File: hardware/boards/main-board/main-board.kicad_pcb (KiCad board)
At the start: 4 copper layers, 292.4 x 42 mm, 142 parts, among them J1 2x12 1.27mm shrouded box head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, J2 1x5, J4 12-way, J5 12-way, J6 8-way 2.54mm right-angle pin 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, Q1 AO3401A, SW1 KS-33, SW2 KS-33, SW3 KS-33, SW4 KS-33, SW5 KS-33, SW6 KS-33, SW7 KS-33, SW8 KS-33, U1 SP0504BAHT or equivalent 4-ch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, U10 MPXV4006DP, U2 MCP3202-CI/SN, U3 OPA2197IDR, U4 REF5050IDR, U5 R-78E5.0-1.0, U6 74AHCT125, U7 74HCS165, U8 74HCS165, U9 SP0504BAHTG 4-channel 5V array

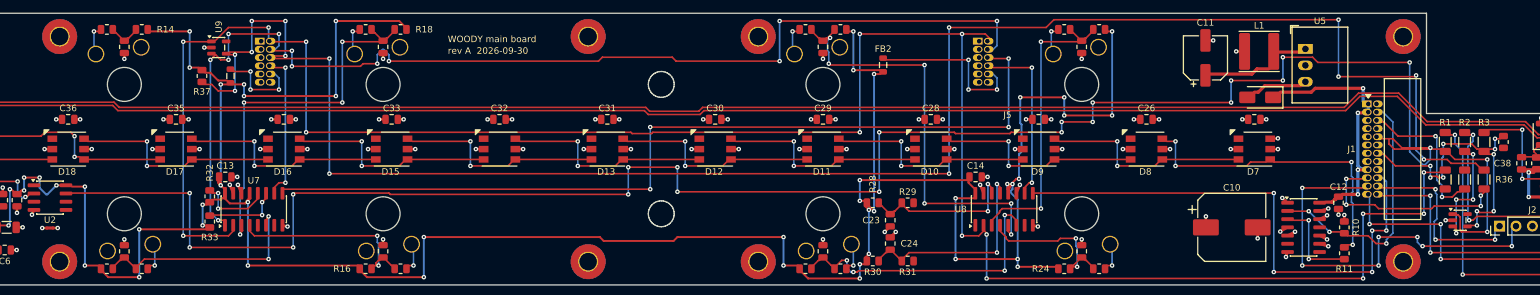
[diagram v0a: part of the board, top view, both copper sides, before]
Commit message: Main board after finish: 12 left
Co-Authored-By: Claude Opus 5.5 <noreply@anthropic.com>
Claude-Session: https://claude.ai/code/session_01LmB4muFXnoLprWX4JzuJ5A
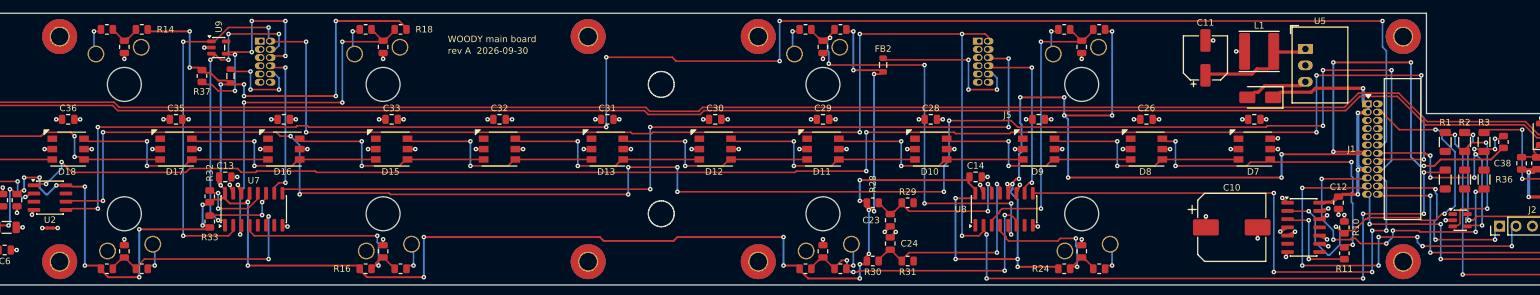
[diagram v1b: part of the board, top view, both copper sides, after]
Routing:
- net /IO35: track 314.6 -> 0.00 mm, vias 22 -> 0
- net /IO37: track 0.00 -> 266.8 mm, vias 0 -> 13
- net /IO36: track 16.3 -> 273.3 mm, vias 4 -> 9
- net /IO39: track 0.00 -> 251.7 mm, vias 0 -> 8
- net /CHAIN_SER_LH: track 280.8 -> 32.0 mm, vias 14 -> 6
- net /CHAIN_SHLD: track 172.6 -> 44.0 mm, vias 12 -> 5
- net DEV_3V3: track 418.1 -> 537.3 mm, vias 48 -> 55
- net /IO7: track 22.3 -> 0.00 mm, vias 2 -> 0
- net /IO1: track 36.7 -> 58.4 mm, vias 3 -> 4
- net /IO33: track 30.3 -> 47.4 mm, vias 4 -> 6
- net /carrier/IO34: track 42.6 -> 40.4 mm, vias 10 -> 8

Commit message: Main board after finish with rip_up 6: 5 left
Co-Authored-By: Claude Opus 5.5 <noreply@anthropic.com>
Claude-Session: https://claude.ai/code/session_01LmB4muFXnoLprWX4JzuJ5A
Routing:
- net /IO35: track 0.00 -> 254.4 mm, vias 0 -> 9
- net /CHAIN_SER_LH: track 32.0 -> 268.6 mm, vias 6 -> 22
- net /CHAIN_SCK: track 321.9 -> 143.2 mm, vias 15 -> 11
- net /CHAIN_SHLD: track 44.0 -> 157.9 mm, vias 5 -> 9
- net /KEY_LT2: track 2.66 -> 55.5 mm, vias 0 -> 4
- net /carrier/IO34: track 40.4 -> 87.9 mm, vias 8 -> 11
- net /IO39: track 251.7 -> 279.5 mm, vias 8 -> 16
- net /IO36: track 273.3 -> 297.4 mm, vias 9 -> 18
- net /IO7: track 0.00 -> 21.5 mm, vias 0 -> 4
- net /IO38: track 0.00 -> 19.5 mm, vias 0 -> 2
- net /IO33: track 47.4 -> 32.1 mm, vias 6 -> 4
- net /U0RXD: track 61.8 -> 49.1 mm
- net /IO37: track 266.8 -> 279.0 mm, vias 13 -> 20
- net /U0TXD: track 27.2 -> 22.4 mm, vias 3 -> 1
- net DEV_3V3: track 537.3 -> 533.5 mm, vias 55 -> 62
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
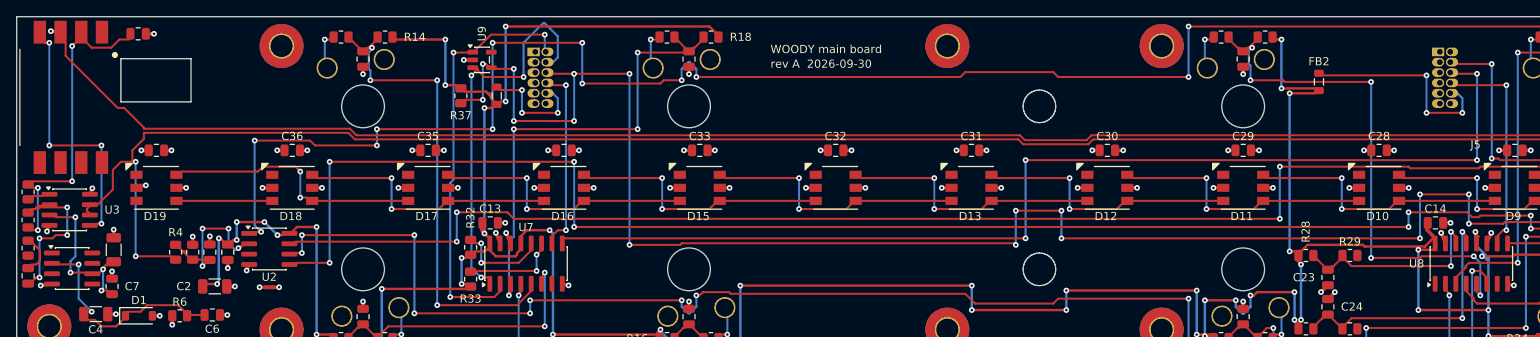
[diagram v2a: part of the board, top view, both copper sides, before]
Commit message: Main board: feedback column stacked as its ring (R7, R9, C9, R8), every connection routed; 3 track-shape errors on CHAIN_SHLD left
Co-Authored-By: Claude Opus 5.5 <noreply@anthropic.com>
Claude-Session: https://claude.ai/code/session_01LmB4muFXnoLprWX4JzuJ5A
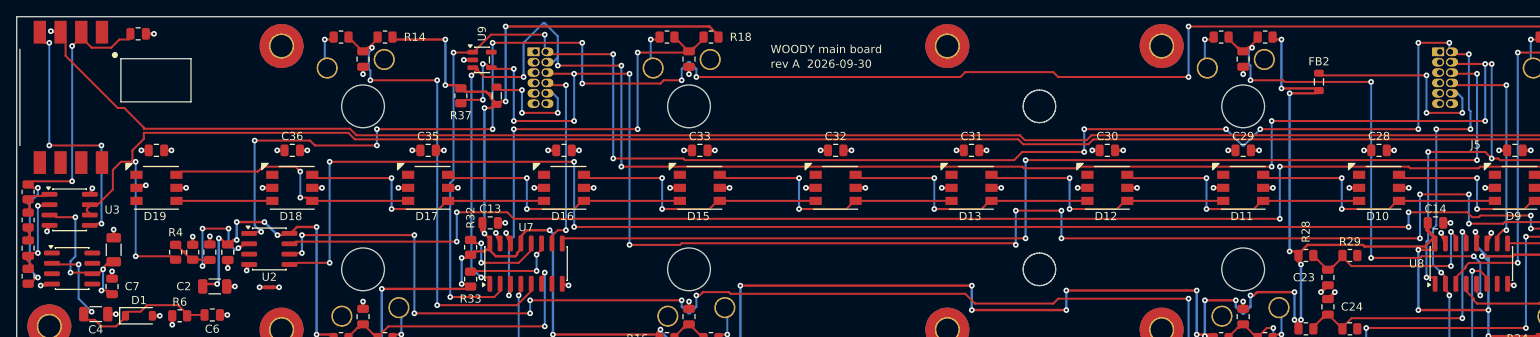
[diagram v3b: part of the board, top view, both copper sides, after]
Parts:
- moved R8 6.90 mm to (68.9, 132.3)
- moved R9 3.45 mm to (68.9, 125.5), turned to -90 degrees
- moved C9 3.40 mm to (68.9, 128.9)
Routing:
- net /CHAIN_SCK: track 143.2 -> 316.7 mm, vias 11 -> 24
- net /CHAIN_SHLD: track 157.9 -> 325.4 mm, vias 9 -> 18
- net /breath-excitation-reference/REF_MINUS: track 18.3 -> 8.13 mm, vias 4 -> 2
- net VS: track 34.2 -> 41.0 mm
- net /breath-excitation-reference/AC_FB_MID: track 3.70 -> 1.05 mm
- net /breath-excitation-reference/BUF_OUT: track 1.20 -> 2.25 mm

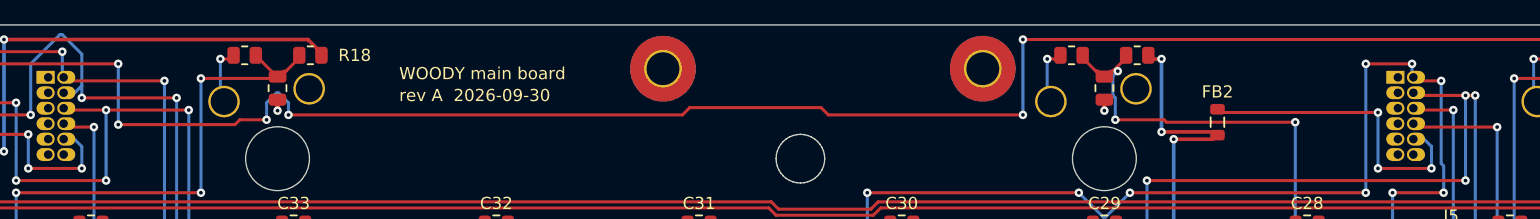
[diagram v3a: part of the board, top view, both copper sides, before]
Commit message: Main board: pcb.py check 0 errors - every connection routed, DRC clean, planes and island checks pass; tidy runs on a fresh load after complete
Co-Authored-By: Claude Opus 5.5 <noreply@anthropic.com>
Claude-Session: https://claude.ai/code/session_01LmB4muFXnoLprWX4JzuJ5A
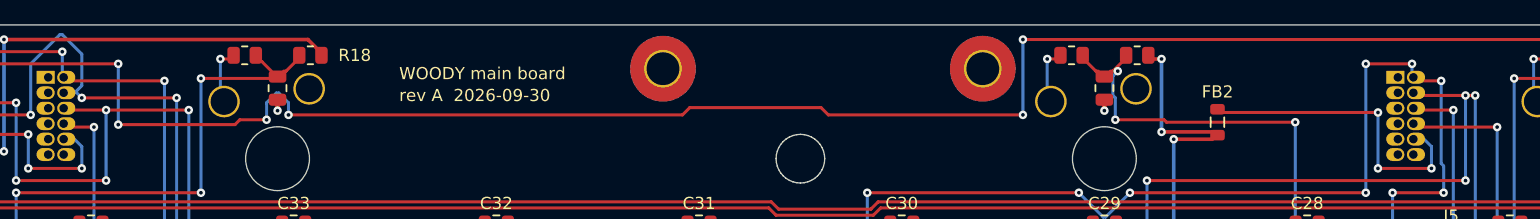
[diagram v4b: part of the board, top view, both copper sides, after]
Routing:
- net /CHAIN_SHLD: track 325.4 -> 321.7 mm
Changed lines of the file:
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@@
-	)
-	(segment
-		(start 247.7 106.3)
-		(end 244.3 106.3)
-		(width 0.25)
-		(layer "F.Cu")
-		(net 6)
 	)
 	(segment
@@
 	(segment
 		(start 133.3 106.1)
-		(end 133.9 105.5)
+		(end 133.4 106)
 		(width 0.25)
 		(layer "B.Cu")
@@
 	)
 	(segment
+		(start 133.4 106)
+		(end 133.9 105.5)
+		(width 0.25)
+		(layer "B.Cu")
+		(net 6)
+	)
+	(segment
 		(start 133.9 105.5)
 		(end 133.9 102.9)
@@
 	)
 	(segment
-		(start 133.9 105.5)
+		(start 133.4 106)
 		(end 133.9 106.5)
 		(width 0.25)

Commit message: Main board re-laid out with the F1 parts: 10 left before finish
Co-Authored-By: Claude Opus 5.5 <noreply@anthropic.com>
Claude-Session: https://claude.ai/code/session_01LmB4muFXnoLprWX4JzuJ5A
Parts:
- added C201: 1uF, Capacitor_SMD:C_0805_2012Metric, F.Cu at (88.9, 102.6)
- added C202: 10nF, Capacitor_SMD:C_0805_2012Metric, F.Cu at (82.4, 102.6)
- added C203: 470pF, Capacitor_SMD:C_0805_2012Metric, F.Cu at (81.8, 126.4)
- added C204: 100nF, Capacitor_SMD:C_0805_2012Metric, F.Cu at (79.2, 125.0)
- moved C8 3.50 mm to (85.9, 102.6)
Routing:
- net /IO36: track 297.4 -> 0.00 mm, vias 18 -> 0
- net /IO37: track 279.0 -> 0.00 mm, vias 20 -> 0
- net /CHAIN_SER_LH: track 268.6 -> 28.0 mm, vias 22 -> 6
- net /IO35: track 254.4 -> 16.6 mm, vias 9 -> 2
- net /carrier/IO34: track 87.9 -> 13.8 mm, vias 11 -> 4
- net /IO39: track 279.5 -> 232.9 mm, vias 16 -> 6
- net /IO33: track 32.1 -> 76.2 mm, vias 4 -> 6
- net /IO1: track 61.6 -> 43.1 mm, vias 7 -> 3
- net /KEY_FREE2: track 10.4 -> 23.4 mm, vias 2 -> 4
- net /U0RXD: track 49.1 -> 61.8 mm
- net /EN: track 37.8 -> 29.4 mm, vias 3 -> 2
- net DEV_3V3: track 533.5 -> 527.0 mm, vias 62 -> 54
- net /CHAIN_SCK: track 316.7 -> 321.9 mm, vias 24 -> 15
- net AGND_INST: track 307.7 -> 312.7 mm, vias 15 -> 19
- net /led-strip-drive/LED_DI: track 45.3 -> 41.5 mm
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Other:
- board text added: "C201"
- board text added: "D4"
- board text added: "FB1"
- board text added: "R35"
- board text added: "U1"
- board text added: "U6"

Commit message: Main board after finish with the F1 parts: 5 left
Co-Authored-By: Claude Opus 5.5 <noreply@anthropic.com>
Claude-Session: https://claude.ai/code/session_01LmB4muFXnoLprWX4JzuJ5A
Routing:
- net /CHAIN_SER_LH: track 28.0 -> 299.8 mm, vias 6 -> 22
- net /IO37: track 0.00 -> 263.0 mm, vias 0 -> 13
- net DEV_3V3: track 527.0 -> 475.0 mm, vias 54 -> 50
- net /IO36: track 0.00 -> 29.7 mm, vias 0 -> 2
- net /carrier/IO34: track 13.8 -> 34.2 mm
- net /IO1: track 43.1 -> 54.7 mm
- net /CHAIN_SHLD: track 318.3 -> 310.8 mm
- net /IO35: track 16.6 -> 21.0 mm
- net /CHAIN_QH_RT: track 81.4 -> 78.9 mm, vias 5 -> 3
- net /U0RXD: track 61.8 -> 63.0 mm, vias 7 -> 5

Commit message: Main board re-laid out with R44: 13 left before finish
Co-Authored-By: Claude Opus 5.5 <noreply@anthropic.com>
Claude-Session: https://claude.ai/code/session_01LmB4muFXnoLprWX4JzuJ5A
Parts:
- added R44: 2k2 1%, Resistor_SMD:R_0603_1608Metric, F.Cu at (136.9, 128.3)
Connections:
- U7 pad 9: /HOP_LT_RH -> /HOP_LT_QH
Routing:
- net /IO37: track 263.0 -> 0.00 mm, vias 13 -> 0
- net /IO35: track 21.0 -> 272.9 mm, vias 2 -> 12
- net /IO36: track 29.7 -> 270.8 mm, vias 2 -> 12
- net /CHAIN_SER_LH: track 299.8 -> 68.3 mm, vias 22 -> 10
- net /CHAIN_SCK: track 321.9 -> 153.7 mm, vias 15 -> 8
- net /CHAIN_SHLD: track 310.8 -> 222.7 mm, vias 26 -> 17
- net /CHAIN_QH_RT: track 78.9 -> 0.00 mm, vias 3 -> 0
- net /KEY_RT2: track 62.6 -> 2.66 mm, vias 6 -> 0
- net /KEY_LT2: track 55.5 -> 2.66 mm, vias 4 -> 0
- net /IO39: track 232.9 -> 272.3 mm, vias 6 -> 12
- net /IO38: track 18.8 -> 44.2 mm, vias 2 -> 3
- net /U0RXD: track 63.0 -> 87.8 mm
- net DEV_3V3: track 475.0 -> 491.7 mm, vias 50 -> 52
- net /IO33: track 76.2 -> 91.0 mm, vias 6 -> 8
- net /KEY_FREE2: track 23.4 -> 10.4 mm, vias 4 -> 2
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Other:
- board text added: "J4"
- board text added: "R44"
- board text removed: "C38"
- board text removed: "R16"
- board text removed: "R28"
- board text removed: "R36"
